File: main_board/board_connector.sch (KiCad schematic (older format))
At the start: 2 parts

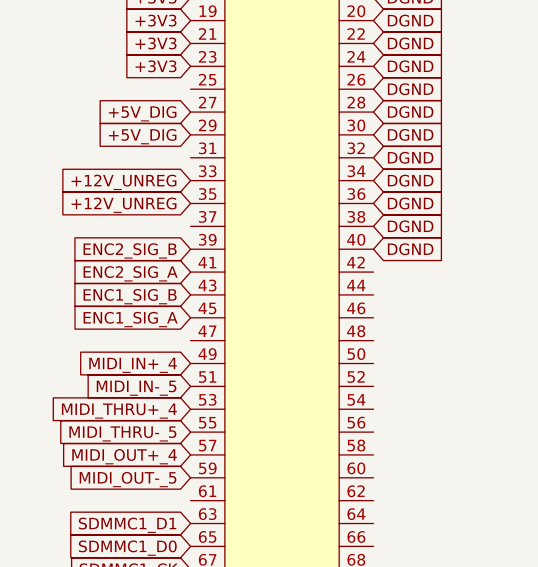
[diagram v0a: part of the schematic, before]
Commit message: Added MIDI connectors and SD card to io_board
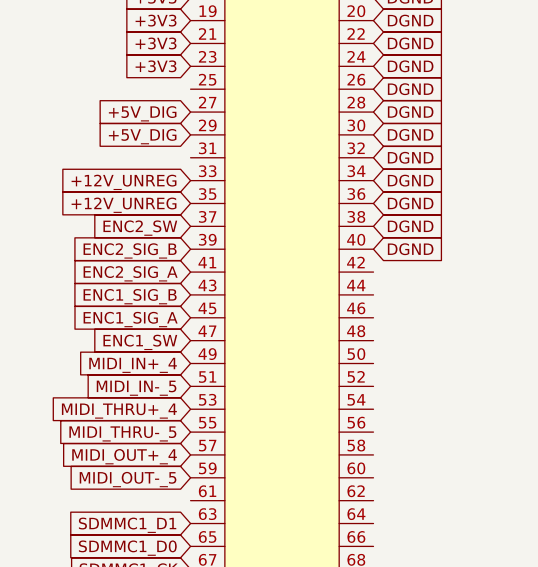
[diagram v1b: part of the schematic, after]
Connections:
- net ENC2_SW: now reaches U?.37
- net ENC1_SW: now reaches U?.47
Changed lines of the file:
@@
 EESchema Schematic File Version 4
 LIBS:main_board-cache
-EELAYER 26 0
+EELAYER 29 0
 EELAYER END
 $Descr A4 11693 8268
 encoding utf-8
-Sheet 13 13
+Sheet 12 12
 Title ""
 Date ""
@@
 Text GLabel 4400 4850 0    50   Input ~ 0
 ACODEC_VIN6+
+Text GLabel 1900 2850 0    50   Input ~ 0
+ENC2_SW
+Text GLabel 1900 3350 0    50   Input ~ 0
+ENC1_SW
 $EndSCHEMATC

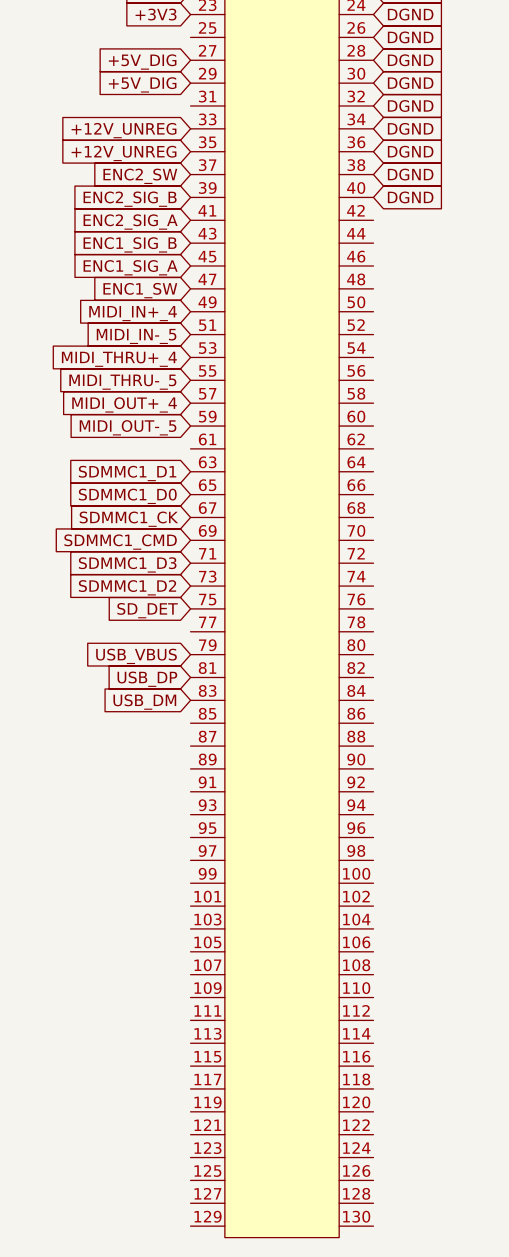
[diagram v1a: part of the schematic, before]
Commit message: Added encoders, started adding CV input stage.
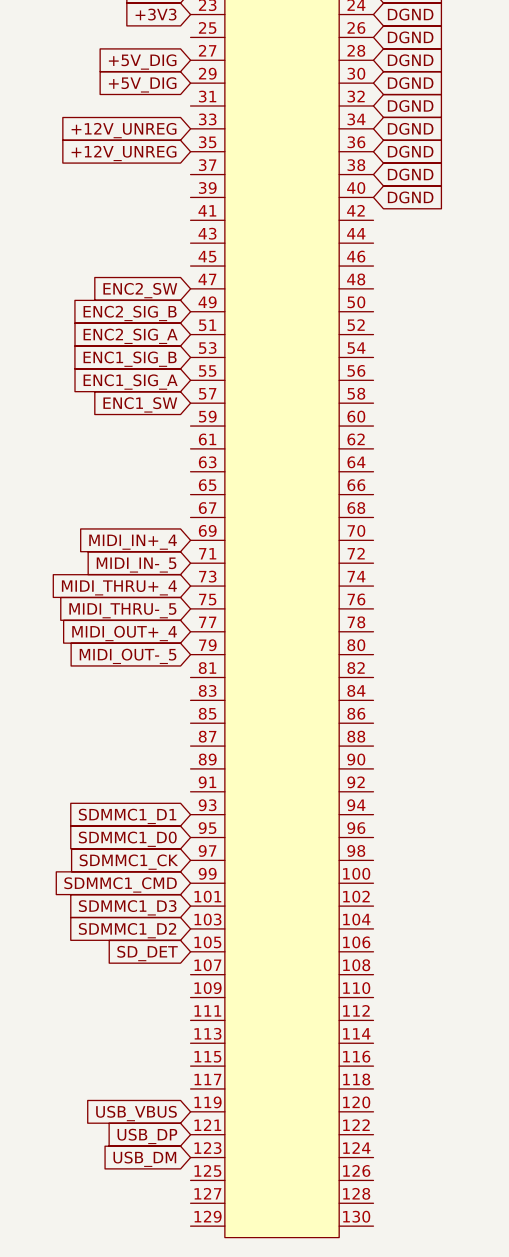
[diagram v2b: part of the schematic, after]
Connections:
- net ENC1_SIG_A: now also U?.55; no longer U?.45
- net ENC1_SIG_B: now also U?.53; no longer U?.43
- net ENC1_SW: now also U?.57; no longer U?.47
- net ENC2_SIG_A: now also U?.51; no longer U?.41
- net ENC2_SIG_B: now also U?.49; no longer U?.39
- net ENC2_SW: now also U?.47; no longer U?.37
- net MIDI_IN+_4: now also U?.69; no longer U?.49
- net MIDI_IN-_5: now also U?.71; no longer U?.51
- net MIDI_OUT+_4: now also U?.77; no longer U?.57
- net MIDI_OUT-_5: now also U?.79; no longer U?.59
- net MIDI_THRU+_4: now also U?.73; no longer U?.53
- net MIDI_THRU-_5: now also U?.75; no longer U?.55
- net SDMMC1_CK: now also U?.97; no longer U?.67
- net SDMMC1_CMD: now also U?.99; no longer U?.69
- net SDMMC1_D0: now also U?.95; no longer U?.65
- net SDMMC1_D1: now also U?.93; no longer U?.63
- net SDMMC1_D2: now also U?.103; no longer U?.73
- net SDMMC1_D3: now also U?.101; no longer U?.71
- net SD_DET: now also U?.105; no longer U?.75
- net USB_DM: now also U?.123; no longer U?.83
- net USB_DP: now also U?.121; no longer U?.81
- net USB_VBUS: now also U?.119; no longer U?.79
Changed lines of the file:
@@
 EESchema Schematic File Version 4
-LIBS:main_board-cache
+LIBS:io_board-cache
 EELAYER 29 0
 EELAYER END
 $Descr A4 11693 8268
 encoding utf-8
-Sheet 12 12
+Sheet 10 11
 Title ""
 Date ""
@@
 Text GLabel 2700 1050 2    50   Input ~ 0
 DGND
-Text GLabel 1900 4150 0    50   Input ~ 0
+Text GLabel 1900 5650 0    50   Input ~ 0
 SDMMC1_D1
-Text GLabel 1900 4250 0    50   Input ~ 0
+Text GLabel 1900 5750 0    50   Input ~ 0
 SDMMC1_D0
-Text GLabel 1900 4350 0    50   Input ~ 0
+Text GLabel 1900 5850 0    50   Input ~ 0
 SDMMC1_CK
+Text GLabel 1900 5950 0    50   Input ~ 0
+SDMMC1_CMD
+Text GLabel 1900 6050 0    50   Input ~ 0
+SDMMC1_D3
+Text GLabel 1900 6150 0    50   Input ~ 0
+SDMMC1_D2
+Text GLabel 1900 6250 0    50   Input ~ 0
+SD_DET
 Text GLabel 1900 4450 0    50   Input ~ 0
-SDMMC1_CMD
+MIDI_IN+_4
 Text GLabel 1900 4550 0    50   Input ~ 0
-SDMMC1_D3
+MIDI_IN-_5
 Text GLabel 1900 4650 0    50   Input ~ 0
-SDMMC1_D2
+MIDI_THRU+_4
 Text GLabel 1900 4750 0    50   Input ~ 0
-SD_DET
+MIDI_THRU-_5
+Text GLabel 1900 4850 0    50   Input ~ 0
+MIDI_OUT+_4
+Text GLabel 1900 4950 0    50   Input ~ 0
+MIDI_OUT-_5
+Text GLabel 1900 3750 0    50   Input ~ 0
+ENC1_SIG_A
+Text GLabel 1900 3650 0    50   Input ~ 0
+ENC1_SIG_B
+Text GLabel 1900 3550 0    50   Input ~ 0
+ENC2_SIG_A
 Text GLabel 1900 3450 0    50   Input ~ 0
-MIDI_IN+_4
-Text GLabel 1900 3550 0    50   Input ~ 0
-MIDI_IN-_5
-Text GLabel 1900 3650 0    50   Input ~ 0
-MIDI_THRU+_4
-Text GLabel 1900 3750 0    50   Input ~ 0
-MIDI_THRU-_5
-Text GLabel 1900 3850 0    50   Input ~ 0
-MIDI_OUT+_4
-Text GLabel 1900 3950 0    50   Input ~ 0
-MIDI_OUT-_5
-Text GLabel 1900 3250 0    50   Input ~ 0
-ENC1_SIG_A
-Text GLabel 1900 3150 0    50   Input ~ 0
-ENC1_SIG_B
-Text GLabel 1900 3050 0    50   Input ~ 0
-ENC2_SIG_A
-Text GLabel 1900 2950 0    50   Input ~ 0
 ENC2_SIG_B
-Text GLabel 1900 5050 0    50   Input ~ 0
+Text GLabel 1900 7050 0    50   Input ~ 0
 USB_DP
-Text GLabel 1900 5150 0    50   Input ~ 0
+Text GLabel 1900 7150 0    50   Input ~ 0
 USB_DM
-Text GLabel 1900 4950 0    50   Input ~ 0
+Text GLabel 1900 6950 0    50   Input ~ 0
 USB_VBUS
 Text GLabel 4400 7450 0    50   Input ~ 0
@@
 Text GLabel 5200 7450 2    50   Input ~ 0
 AGND
+Text GLabel 1900 3350 0    50   Input ~ 0
+ENC2_SW
+Text GLabel 1900 3850 0    50   Input ~ 0
+ENC1_SW
+Text GLabel 4400 4850 0    50   Input ~ 0
+ACODEC_VIN6+
+Text GLabel 4400 4750 0    50   Input ~ 0
+ACODEC_VIN6-
+Text GLabel 4400 4650 0    50   Input ~ 0
+ACODEC_VIN5+
+Text GLabel 4400 4550 0    50   Input ~ 0
+ACODEC_VIN5-
+Text GLabel 4400 4450 0    50   Input ~ 0
+ACODEC_VIN4+
+Text GLabel 4400 4350 0    50   Input ~ 0
+ACODEC_VIN4-
+Text GLabel 4400 4250 0    50   Input ~ 0
+ACODEC_VIN3+
+Text GLabel 4400 4150 0    50   Input ~ 0
+ACODEC_VIN3-
+Text GLabel 4400 4050 0    50   Input ~ 0
+ACODEC_VIN2+
+Text GLabel 4400 3950 0    50   Input ~ 0
+ACODEC_VIN2-
+Text GLabel 4400 3850 0    50   Input ~ 0
+ACODEC_VIN1+
+Text GLabel 4400 3750 0    50   Input ~ 0
+ACODEC_VIN1-
+Text GLabel 4400 5050 0    50   Input ~ 0
+ACODEC_VOUT8+
+Text GLabel 4400 5150 0    50   Input ~ 0
+ACODEC_VOUT8-
+Text GLabel 4400 5250 0    50   Input ~ 0
+ACODEC_VOUT7+
+Text GLabel 4400 5350 0    50   Input ~ 0
+ACODEC_VOUT7-
+Text GLabel 4400 5450 0    50   Input ~ 0
+ACODEC_VOUT6+
+Text GLabel 4400 5550 0    50   Input ~ 0
+ACODEC_VOUT6-
+Text GLabel 4400 5650 0    50   Input ~ 0
+ACODEC_VOUT5+
+Text GLabel 4400 5750 0    50   Input ~ 0
+ACODEC_VOUT5-
+Text GLabel 4400 5850 0    50   Input ~ 0
+ACODEC_VOUT4+
+Text GLabel 4400 5950 0    50   Input ~ 0
+ACODEC_VOUT4-
+Text GLabel 4400 6050 0    50   Input ~ 0
+ACODEC_VOUT3+
+Text GLabel 4400 6150 0    50   Input ~ 0
+ACODEC_VOUT3-
+Text GLabel 4400 6250 0    50   Input ~ 0
+ACODEC_VOUT2+
+Text GLabel 4400 6350 0    50   Input ~ 0
+ACODEC_VOUT2-
+Text GLabel 4400 6450 0    50   Input ~ 0
+ACODEC_VOUT1+
 Text GLabel 4400 6550 0    50   Input ~ 0
 ACODEC_VOUT1-
-Text GLabel 4400 6450 0    50   Input ~ 0
-ACODEC_VOUT1+
-Text GLabel 4400 6350 0    50   Input ~ 0
-ACODEC_VOUT2-
-Text GLabel 4400 6250 0    50   Input ~ 0
-ACODEC_VOUT2+
-Text GLabel 4400 6150 0    50   Input ~ 0
-ACODEC_VOUT3-
-Text GLabel 4400 6050 0    50   Input ~ 0
-ACODEC_VOUT3+
-Text GLabel 4400 5950 0    50   Input ~ 0
-ACODEC_VOUT4-
-Text GLabel 4400 5850 0    50   Input ~ 0
-ACODEC_VOUT4+
-Text GLabel 4400 5750 0    50   Input ~ 0
-ACODEC_VOUT5-
-Text GLabel 4400 5650 0    50   Input ~ 0
-ACODEC_VOUT5+
-Text GLabel 4400 5550 0    50   Input ~ 0
-ACODEC_VOUT6-
-Text GLabel 4400 5450 0    50   Input ~ 0
-ACODEC_VOUT6+
-Text GLabel 4400 5350 0    50   Input ~ 0
-ACODEC_VOUT7-
-Text GLabel 4400 5250 0    50   Input ~ 0
-ACODEC_VOUT7+
-Text GLabel 4400 5150 0    50   Input ~ 0
-ACODEC_VOUT8-
-Text GLabel 4400 5050 0    50   Input ~ 0
-ACODEC_VOUT8+
-Text GLabel 4400 3750 0    50   Input ~ 0
-ACODEC_VIN1-
-Text GLabel 4400 3850 0    50   Input ~ 0
-ACODEC_VIN1+
-Text GLabel 4400 3950 0    50   Input ~ 0
-ACODEC_VIN2-
-Text GLabel 4400 4050 0    50   Input ~ 0
-ACODEC_VIN2+
-Text GLabel 4400 4150 0    50   Input ~ 0
-ACODEC_VIN3-
-Text GLabel 4400 4250 0    50   Input ~ 0
-ACODEC_VIN3+
-Text GLabel 4400 4350 0    50   Input ~ 0
-ACODEC_VIN4-
-Text GLabel 4400 4450 0    50   Input ~ 0
-ACODEC_VIN4+
-Text GLabel 4400 4550 0    50   Input ~ 0
-ACODEC_VIN5-
-Text GLabel 4400 4650 0    50   Input ~ 0
-ACODEC_VIN5+
-Text GLabel 4400 4750 0    50   Input ~ 0
-ACODEC_VIN6-
-Text GLabel 4400 4850 0    50   Input ~ 0
-ACODEC_VIN6+
-Text GLabel 1900 2850 0    50   Input ~ 0
-ENC2_SW
-Text GLabel 1900 3350 0    50   Input ~ 0
-ENC1_SW
 $EndSCHEMATC
